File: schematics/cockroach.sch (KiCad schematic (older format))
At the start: 0 parts

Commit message: Added SD card and GPS breakout board symbols
Connected the micro SD Card and the GPS breakout board to Ardiuno Nano. Not sure on sending the bus signals from 3.3V to 5V voltage levels so copied M4 Avionics
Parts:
- added A1: Arduino_Nano_v2.x, Module:Arduino_Nano, symbol MCU_Module:Arduino_Nano_v2.x
- added J1: Conn_01x08_Male, symbol Connector:Conn_01x08_Male
- added R? (x4): R, symbol Device:R
- added U1: MICROSD, cusf:MICROSD_MOLEX_503398-1892, symbol cusf-kicad:MICROSD
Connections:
- new net +3V3: A1.17 (3V3), J1.1 (Pin_1), R?.1, R?.1, R?.1, R?.1, U1.4 (VDD)
- new net GND: A1.29 (GND), A1.4 (GND), J1.2 (Pin_2), U1.6 (VSS), U1.9 (SHIELD)
- new net MISO: A1.15 (D12), R?.2, U1.7 (DAT0)
- new net MOSI: A1.14 (D11), R?.2, U1.3 (CMD)
- new net RX0: A1.2 (D0/RX), J1.5 (Pin_5)
- new net SCK: A1.16 (D13), R?.2, U1.5 (CLK)
- new net SCL: J1.7 (Pin_7)
- new net SDA: J1.8 (Pin_8)
- new net SS: A1.13 (D10), R?.2, U1.2 (DAT3)
- new net TP: A1.5 (D2), J1.4 (Pin_4)
- new net TX0: A1.1 (D1/TX), J1.6 (Pin_6)
- no-connect marks 0 -> 7

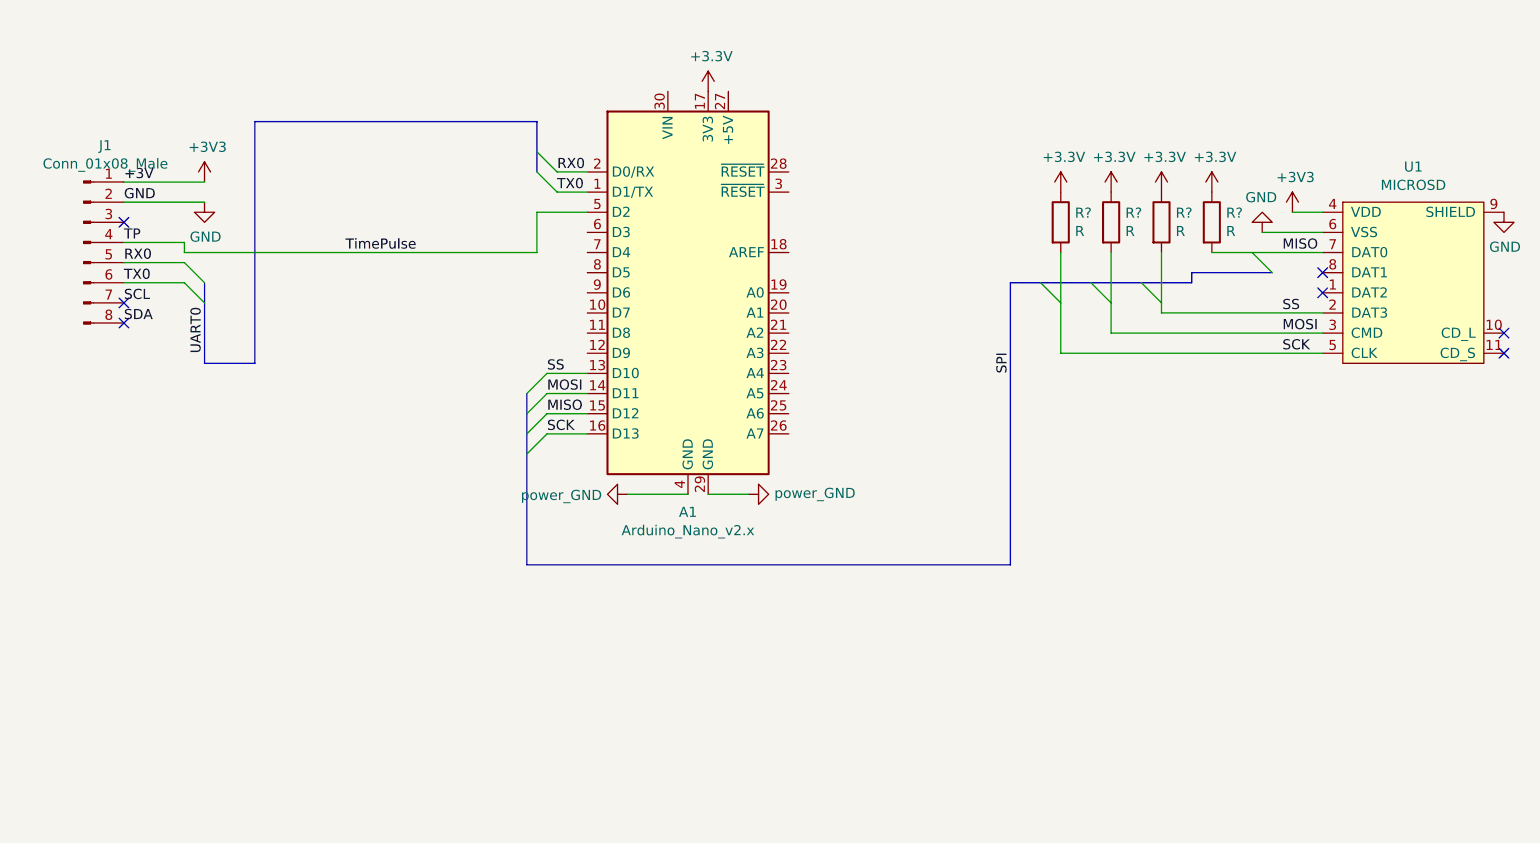
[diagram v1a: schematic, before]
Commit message: Added Level shifter
Fixed hardcoded library but forking cusf kicad

Fixed UART misconnection

Added the CD74HC4050 to be used as an buffer for the SPI and UART connections. The document I used also uses a 3v3 voltage regulator but considering we are powering from our own 3v3 supply we should be fine.

I have added the 74HC4050 as a lib folder separately. Once it's merged into cusf-kicad I will delete this file.
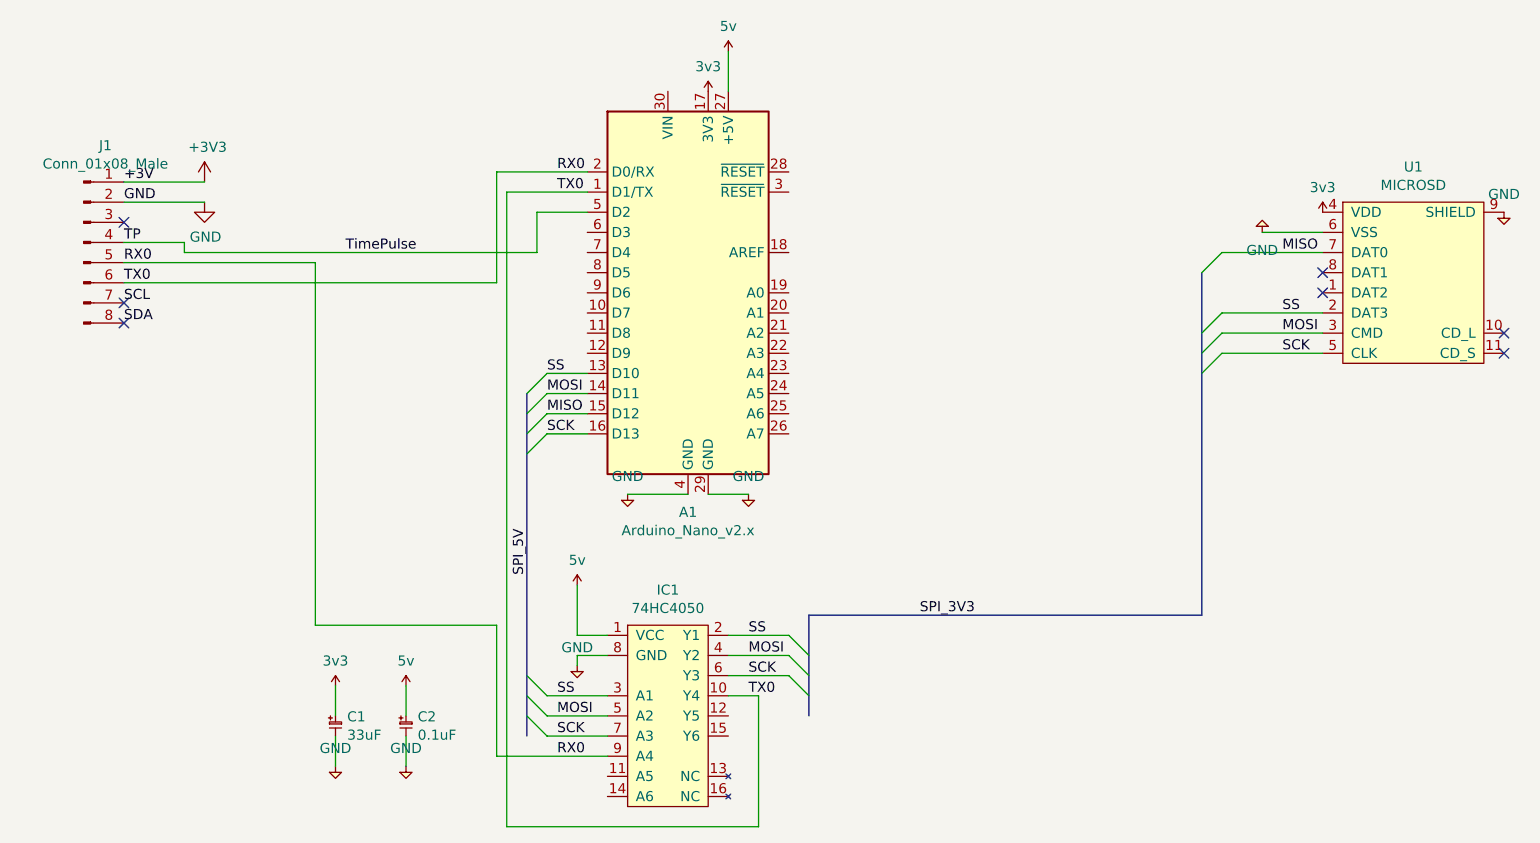
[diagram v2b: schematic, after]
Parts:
- removed R? (x4): R, symbol Device:R
- added C1: 33uF, symbol cusf-kicad:CP
- added C2: 0.1uF, symbol cusf-kicad:CP
- added IC1: 74HC4050, cusf:soic-16, symbol 74hc4050:74HC4050
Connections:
- net TX0 is gone; now on net RX0: A1.1 (D1/TX), J1.6 (Pin_6)
- net +3V3: no longer A1.17 (3V3), U1.4 (VDD)
- net GND: now also C1.1, C2.1, IC1.8 (GND)
- net MOSI: now also IC1.4 (Y2), IC1.5 (A2)
- net RX0: now also IC1.10 (Y4), IC1.9 (A4)
- net SCK: now also IC1.6 (Y3), IC1.7 (A3)
- net SS: now also IC1.2 (Y1), IC1.3 (A1)
- net 5v: now reaches A1.27 (+5V)
- net 5v: now also C2.2, IC1.1 (VCC)
- new net 3v3: A1.17 (3V3), C1.2, U1.4 (VDD)

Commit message: Fix symbol libraries (some symbols still missing)
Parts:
- removed J1: Conn_01x08_Male, symbol Connector:Conn_01x08_Male
- added J?: CONN_01x08, symbol cusf-kicad:CONN_01x08
- A1: symbol MCU_Module:Arduino_Nano_v2.x -> cockroach-rescue:Arduino_Nano_v2.x-MCU_Module
- C1, C2: symbol cusf-kicad:CP -> cusf-kicad:C
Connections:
- net labels removed: +3V3
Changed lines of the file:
@@
 EESchema Schematic File Version 4
-EELAYER 30 0
+LIBS:cockroach-cache
+EELAYER 26 0
 EELAYER END
 $Descr A4 11693 8268
@@
 Comment4 ""
 $EndDescr
-$Comp
-L Connector:Conn_01x08_Male J1
-U 1 1 60537954
-P 2850 2450
-F 0 "J1" H 2958 2931 50  0000 C CNN
-F 1 "Conn_01x08_Male" H 2958 2840 50  0000 C CNN
-F 2 "" H 2850 2450 50  0001 C CNN
-F 3 "~" H 2850 2450 50  0001 C CNN
-	1    2850 2450
-	1    0    0    -1
-$EndComp
-Text Label 3050 2850 0    50   ~ 0
+Text Label 2850 2850 0    50   ~ 0
 SDA
-Text Label 3050 2750 0    50   ~ 0
+Text Label 2850 2750 0    50   ~ 0
 SCL
 Text Label 3050 2650 0    50   ~ 0
@@
 GND
 $Comp
-L power:+3V3 #PWR01
-U 1 1 6054D03D
-P 3450 2150
-F 0 "#PWR01" H 3450 2000 50  0001 C CNN
-F 1 "+3V3" H 3465 2323 50  0000 C CNN
-F 2 "" H 3450 2150 50  0001 C CNN
-F 3 "" H 3450 2150 50  0001 C CNN
-	1    3450 2150
-	1    0    0    -1
-$EndComp
-Wire Wire Line
-	3050 2150 3450 2150
-$Comp
-L power:GND #PWR02
+L cusf-kicad:GND #PWR02
 U 1 1 6054DD2D
 P 3450 2250
@@
 	1    0    0    -1
 $EndComp
-Wire Wire Line
-	3050 2250 3450 2250
 Text Label 5200 2100 0    50   ~ 0
 RX0
@@
 Wire Wire Line
 	9000 2400 8700 2400
-NoConn ~ 3050 2750
-NoConn ~ 3050 2850
-NoConn ~ 3050 2350
+NoConn ~ 2850 2750
+NoConn ~ 2850 2850
 Wire Wire Line
 	3350 2450 3350 2500
-Wire Wire Line
-	3050 2450 3350 2450
 Wire Wire Line
 	3350 2500 5100 2500
@@
 Wire Wire Line
 	5350 3200 5150 3200
-Wire Wire Line
-	3050 2550 4000 2550
-$Comp
-L MCU_Module:Arduino_Nano_v2.x A1
+$Comp
+L cockroach-rescue:Arduino_Nano_v2.x-MCU_Module A1
 U 1 1 60451EC5
 P 5850 2700
@@
 $EndComp
 $Comp
-L cusf-kicad:CP C1
+L cusf-kicad:C C1
 U 1 1 60813A2C
 P 4100 4900
@@
 $EndComp
 $Comp
-L cusf-kicad:CP C2
+L cusf-kicad:C C2
 U 1 1 608146EF
 P 4450 4900
@@
 	4900 2100 4900 2650
 Wire Wire Line
-	3050 2650 4900 2650
-Wire Wire Line
 	4000 2550 4000 4350
 Wire Wire Line
@@
 Wire Wire Line
 	4950 2200 5350 2200
+Text Label 6150 4700 0    50   ~ 0
+TX0
+Text Label 5200 5000 0    50   ~ 0
+RX0
+$Comp
+L cusf-kicad:3v3 #PWR?
+U 1 1 6091DF98
+P 3450 2150
+F 0 "#PWR?" H 3450 2260 50  0001 L CNN
+F 1 "3v3" H 3450 2274 50  0000 C CNN
+F 2 "" H 3450 2150 50  0001 C CNN
+F 3 "" H 3450 2150 50  0001 C CNN
+	1    3450 2150
+	1    0    0    -1
+$EndComp
+$Comp
+L cusf-kicad:CONN_01x08 J?
+U 1 1 6091E2D2
+P 2750 2150
+F 0 "J?" H 2781 2365 50  0000 C CNN
+F 1 "CONN_01x08" H 2781 2274 50  0000 C CNN
+F 2 "" H 2750 2150 50  0001 C CNN
+F 3 "" H 2750 2150 50  0001 C CNN
+	1    2750 2150
+	1    0    0    -1
+$EndComp
+Wire Wire Line
+	2850 2150 3450 2150
+Wire Wire Line
+	2850 2250 3450 2250
+Wire Wire Line
+	2850 2450 3350 2450
+Wire Wire Line
+	2850 2550 4000 2550
+Wire Wire Line
+	2850 2650 4900 2650
+NoConn ~ 2850 2350
 Wire Bus Line
 	8400 2600 8400 4300
@@
 Wire Bus Line
 	5050 3200 5050 4900
-Text Label 6150 4700 0    50   ~ 0
-TX0
-Text Label 5200 5000 0    50   ~ 0
-RX0
 $EndSCHEMATC
